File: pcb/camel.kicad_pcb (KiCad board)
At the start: 4 copper layers, 55 x 28 mm, 58 parts, among them J1 Conn_01x04, J2 Conn_01x04, J3 TC2030-NL, J4 USART, J5 Conn_01x04, J6 I2C STEMMA, U1 MCP1700T-3302E/TT, U2 HX712, U3 STM32L031F6P6, U4 HX712

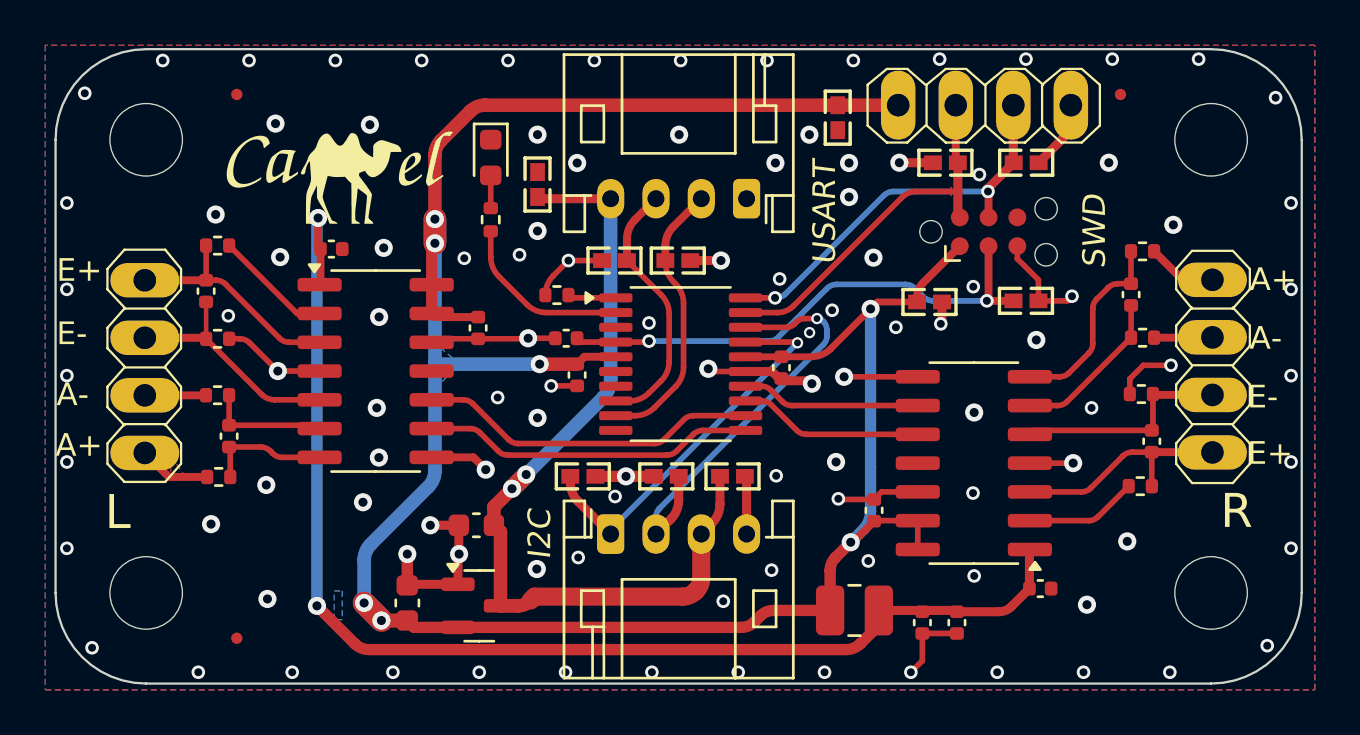
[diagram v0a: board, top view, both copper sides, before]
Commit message: Update to STM32L071 and FreeRTOS, first stage
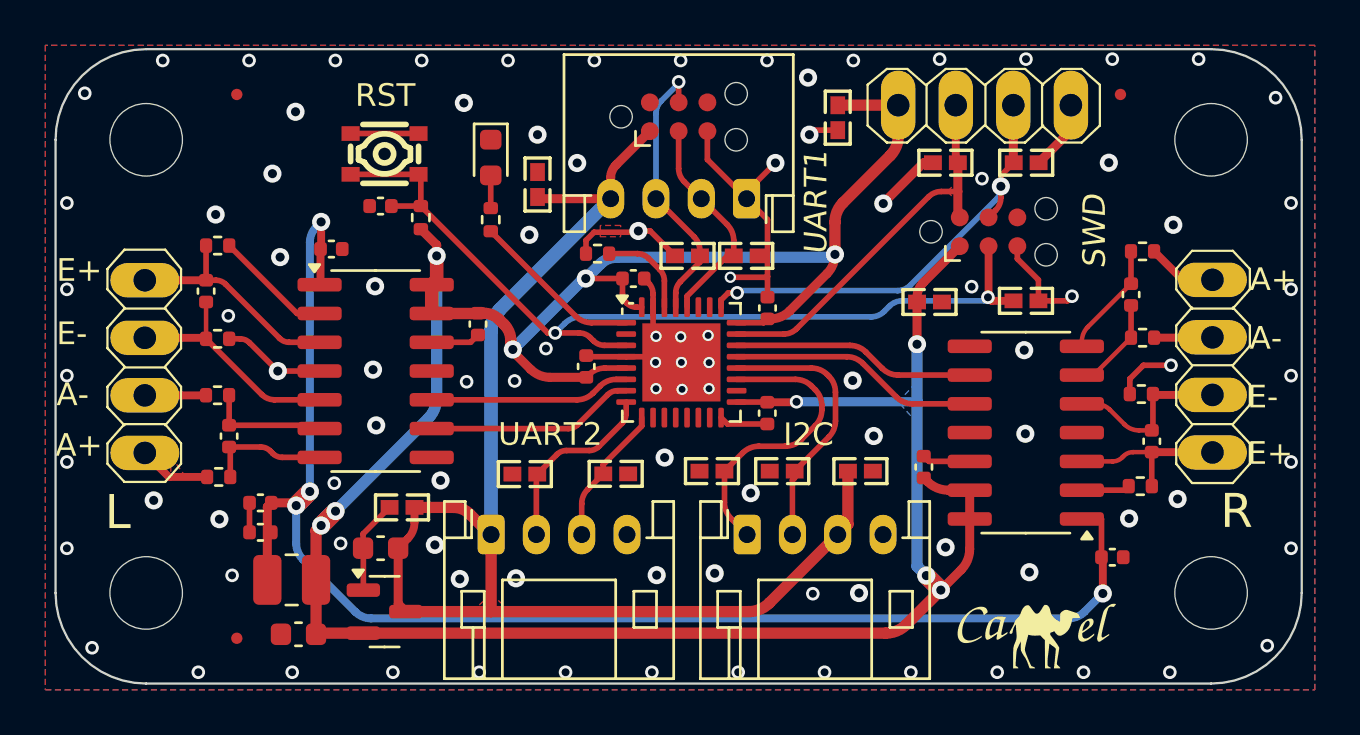
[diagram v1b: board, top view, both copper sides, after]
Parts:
- removed the G*** at (133.6, 96.7)
- removed REF01: QR, camel:camel_qrcode_5x5
- added C16: 100n, Capacitor_SMD:C_0402_1005Metric, F.Cu at (152.4, 107.1)
- added C17: 100n, Capacitor_SMD:C_0402_1005Metric, F.Cu at (146.5, 101.1)
- added D13: RCLAMP0521P-N, camel:X1-DFN1006-2_L1.0-W0.6-BI, F.Cu at (136.3, 111.2)
- added D14: RCLAMP0521P-N, camel:X1-DFN1006-2_L1.0-W0.6-BI, F.Cu at (145.7, 109.7)
- added D15: RCLAMP0521P-N, camel:X1-DFN1006-2_L1.0-W0.6-BI, F.Cu at (141.7, 109.8)
- added G3: LOGO, camel:camel_logo_7, F.Cu at (164.3, 116.9)
- added J7: UART2, Connector_JST:JST_PH_S4B-PH-K_1x04_P2.00mm_Horizontal, F.Cu at (140.2, 112.4)
- added QR1: QR, camel:camel_qrcode_5x5, B.Cu at (163.5, 111.0)
- added R11: 10K, Resistor_SMD:R_0402_1005Metric, F.Cu at (137.1, 98.4)
- added SW1: RESET, camel:SW-SMD_4P-L3.0-W2.6-P1.80-LS3.5, F.Cu at (135.5, 95.6)
- J4: value USART -> UART1; footprint Connector_JST:JST_PH_S4B-PH-K_1x04_P2.00mm_Horizontal -> camel:JST_PH_S4B-PH-K_1x04_P2.00mm_Horizontal_TC-2030-IDC-NL_2x03_P1.27mm_Vertical
- U3: value STM32L031F6P6 -> STM32L071KBU6; footprint Package_SO:TSSOP-20_4.4x6.5mm_P0.65mm -> Package_DFN_QFN:QFN-32-1EP_5x5mm_P0.5mm_EP3.45x3.45mm
- moved C3 31.2 mm to (130.0, 111.0), turned to 180 degrees
- moved C4 29.5 mm to (130.0, 112.3), turned to 180 degrees
- moved L1 24.9 mm to (131.4, 114.4), turned to 0 degrees
- moved C13 10.1 mm to (135.3, 97.9)
- moved J6 6.02 mm to (151.5, 112.4)
- moved D10 5.70 mm to (150.0, 109.6), turned to 0 degrees
- moved D11 5.65 mm to (156.5, 109.6)
- moved D9 5.12 mm to (153.1, 109.6)
- moved C6 5.00 mm to (131.7, 116.8), turned to 180 degrees
- moved C5 4.35 mm to (135.3, 113.0)
- moved U1 4.19 mm to (135.5, 115.8)
- moved C1 3.47 mm to (167.6, 113.4)
- moved D8 3.23 mm to (148.9, 100.1)
- moved D7 3.03 mm to (151.5, 100.1)
- moved C9 2.91 mm to (159.3, 109.4)
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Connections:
- D7 pad 2: /USART_RX -> /USART1_TX
- D8 pad 2: /USART_TX -> /USART1_RX
- J4 pad 2: /USART_RX -> /USART1_TX
- J4 pad 3: /USART_TX -> /USART1_RX
- U3 pad 1: /BOOT0 -> /LED1
- U3 pad 11: /SCK1 -> unconnected-(U3-PA5-Pad11)
- U3 pad 12: /DOUT1 -> unconnected-(U3-PA6-Pad12)
- U3 pad 13: /DOUT2 -> unconnected-(U3-PA7-Pad13)
- U3 pad 14: /SCK2 -> unconnected-(U3-PB0-Pad14)
- U3 pad 15: GND -> unconnected-(U3-PB1-Pad15)
- U3 pad 16: +3V3 -> GND
- U3 pad 17: /I2C_SCL -> +3V3
- U3 pad 18: /I2C_SDA -> unconnected-(U3-PA8-Pad18)
- U3 pad 19: /SWDIO -> /I2C_SCL
- U3 pad 2: /LED1 -> unconnected-(U3-PC15-Pad2)
- U3 pad 20: /SWCLK -> /I2C_SDA
- U3 pad 3: unconnected-(U3-PC15-Pad3) -> /NRST
- U3 pad 4: /NRST -> GND
- U3 pad 6: unconnected-(U3-PA0-Pad6) -> /DOUT1
- U3 pad 7: unconnected-(U3-PA1-Pad7) -> /SCK1
- U3 pad 8: /USART_TX -> /USART2_TX
- U3 pad 9: /USART_RX -> /USART2_RX
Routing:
- net VDD: track 38.5 -> 59.5 mm, vias 2 -> 0
- net +3V3: track 110.7 -> 130.4 mm, vias 7 -> 10
- net /NRST: track 23.0 -> 40.3 mm
- net /USART1_RX: track 0.00 -> 13.1 mm, vias 0 -> 1
- net /USART_TX: track 12.3 -> 0.00 mm
- net /USART_RX: track 12.3 -> 0.00 mm
- net /USART1_TX: track 0.00 -> 9.71 mm
- net VDDA: track 55.5 -> 64.5 mm, vias 2 -> 4
- net /USART2_TX: track 0.00 -> 8.28 mm
- net /I2C_SDA: track 19.0 -> 12.0 mm, vias 1 -> 0
- net /USART2_RX: track 0.00 -> 6.22 mm
- net /DOUT1: track 15.0 -> 8.86 mm
- net /SCK1: track 14.7 -> 9.22 mm
- net GND: track 61.8 -> 57.2 mm, vias 108 -> 99
- net /I2C_SCL: track 17.4 -> 13.3 mm, vias 1 -> 0
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- added copper zone on F.Cu, net VDD
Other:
- board text added: "RST"
- board text added: "UART1"
- board text added: "UART2"
- board text removed: "USART"
